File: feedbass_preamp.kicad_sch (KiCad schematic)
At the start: 15 parts, among them J2 Conn_Coaxial, U7 Opamp_Dual

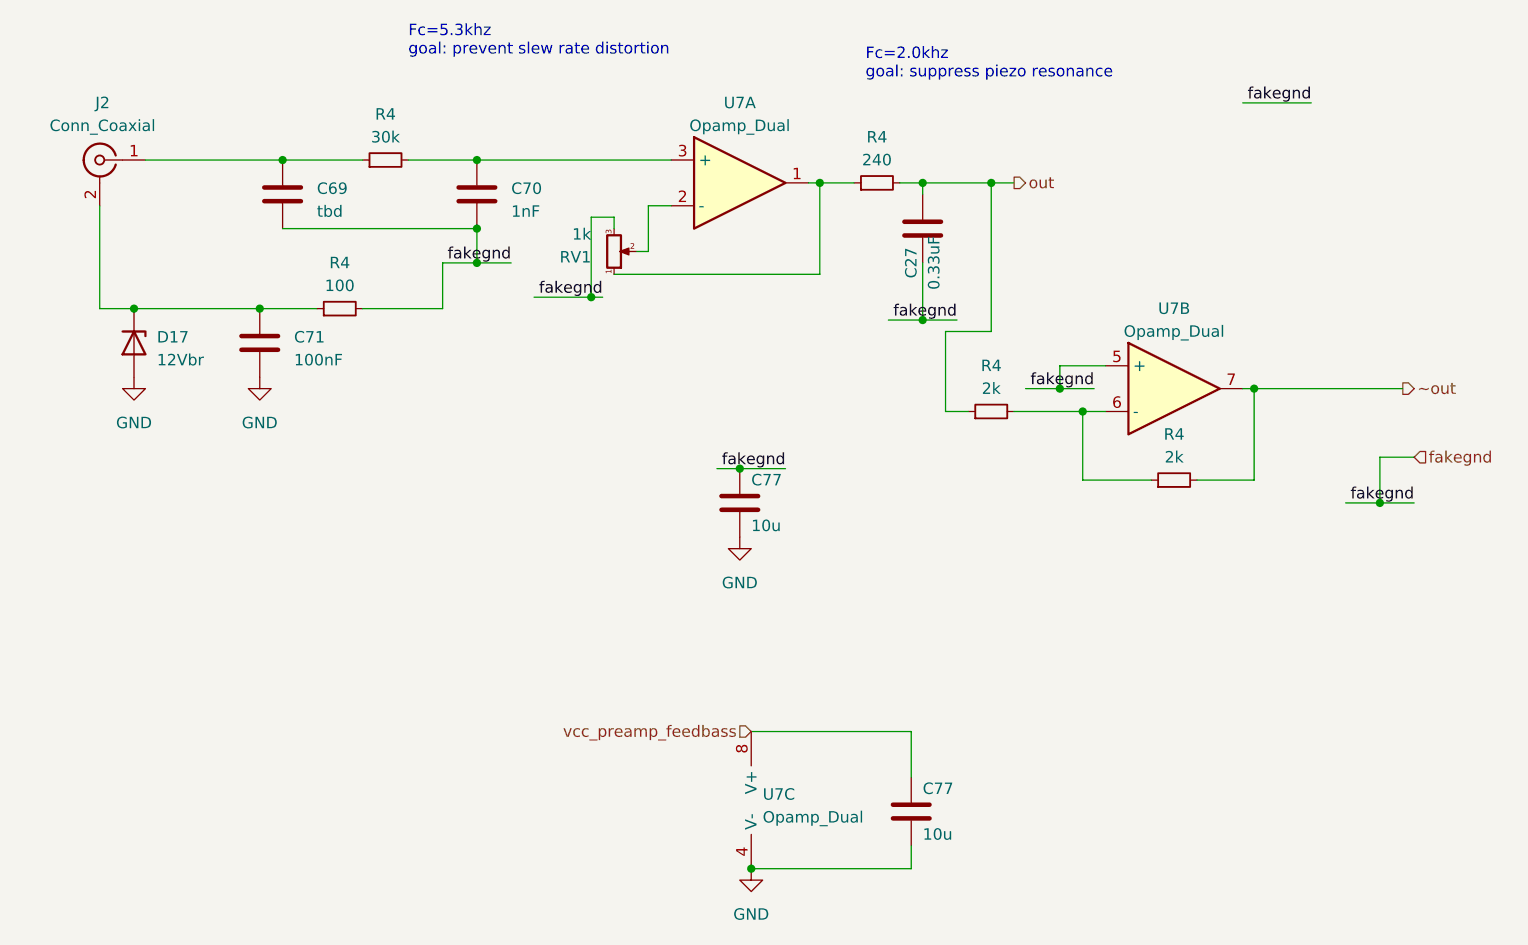
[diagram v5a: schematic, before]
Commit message: update to kicad 8
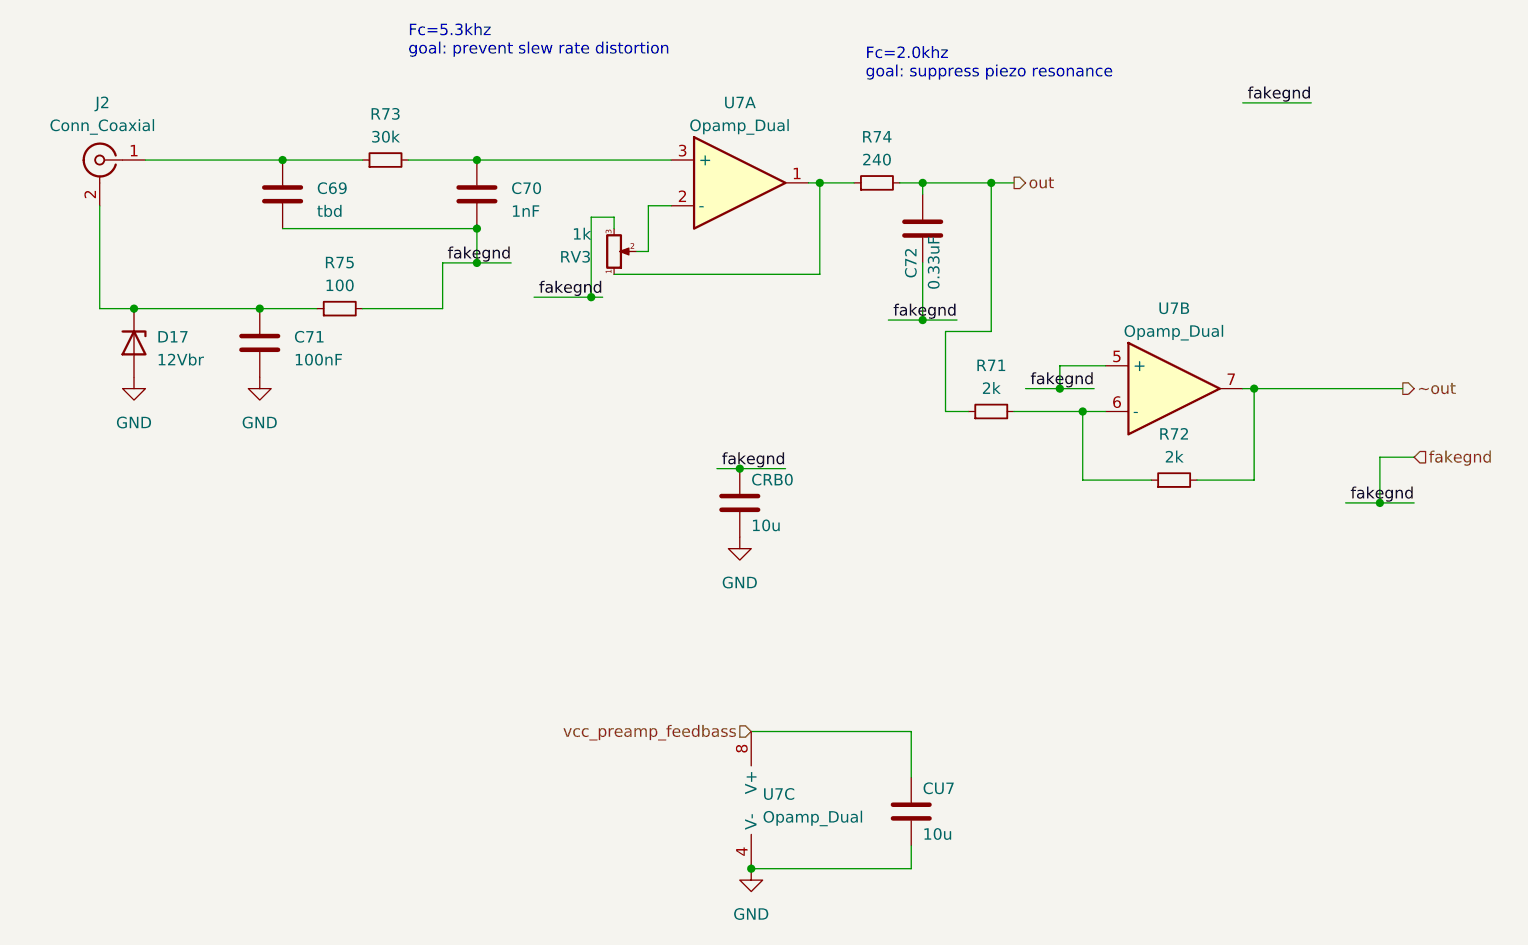
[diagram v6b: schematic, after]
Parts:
- renumbered C27 to C72, C77 to CRB0, C77 to CU7, R4 to R71, R4 to R72, R4 to R73, R4 to R74, R4 to R75, RV1 to RV3
